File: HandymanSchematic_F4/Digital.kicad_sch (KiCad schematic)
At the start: 39 parts, among them J1 SWD Header, J2 JACKS, J5 ScopeGroundLoop, Q2 2N7002, Q3 2N7002, SW1 RST, SW2 BYP, U3 STM32F411RETx, U4 AMS1117, U5 SSD1306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

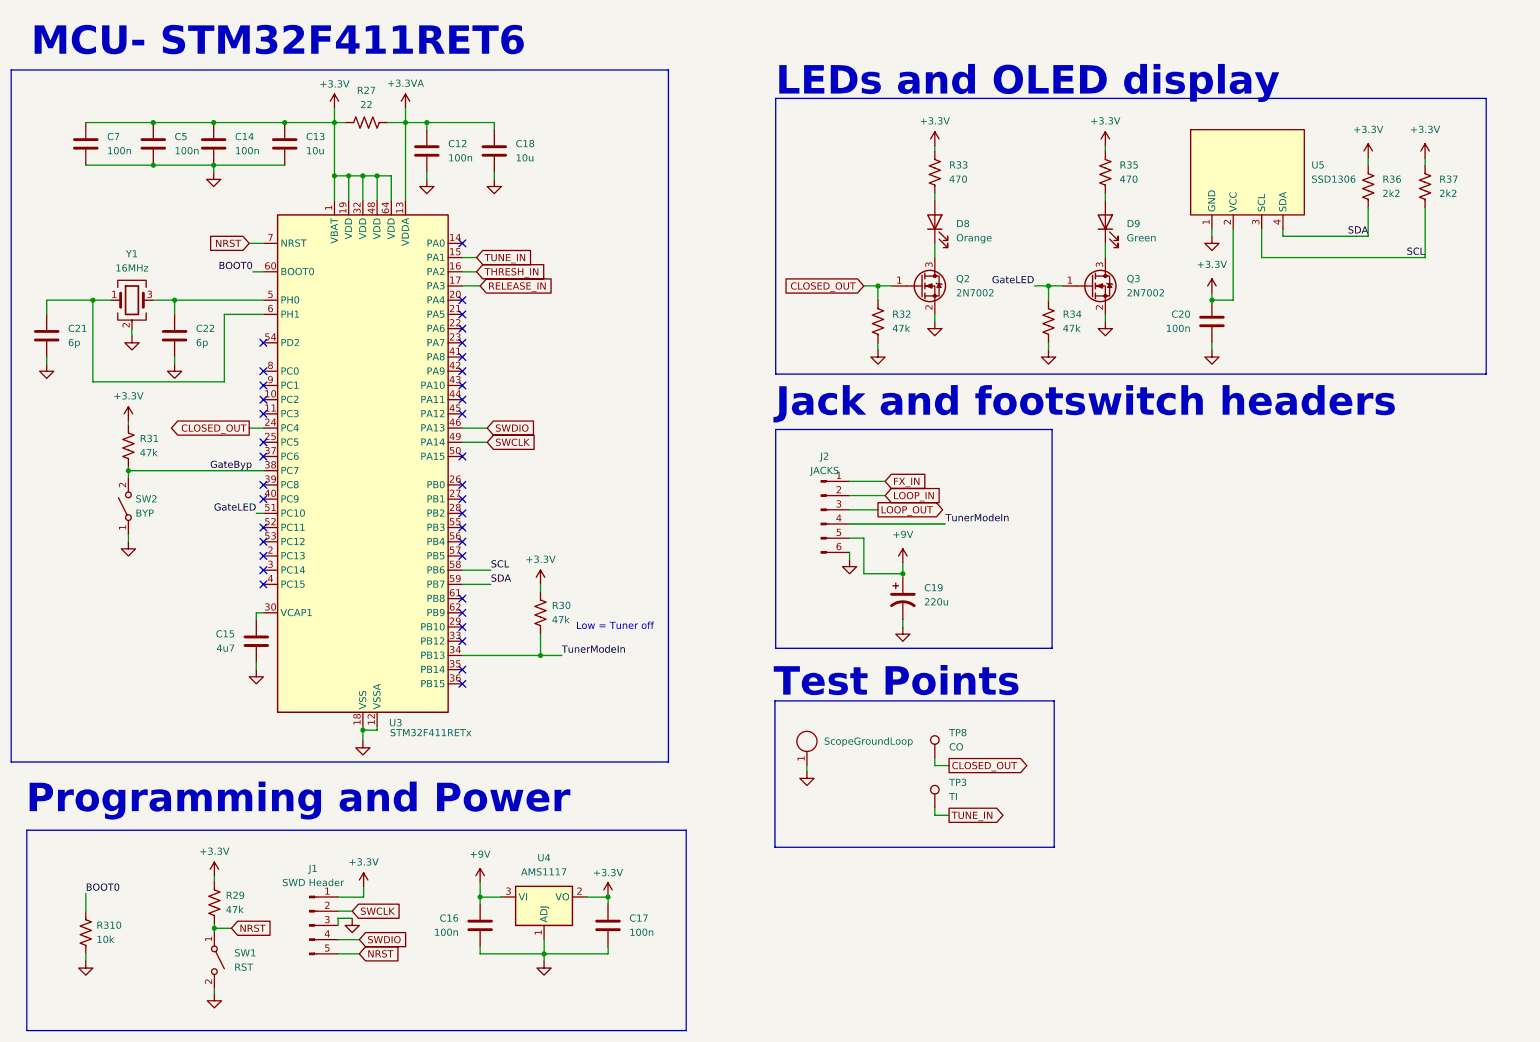
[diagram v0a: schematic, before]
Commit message: schem changes for new display
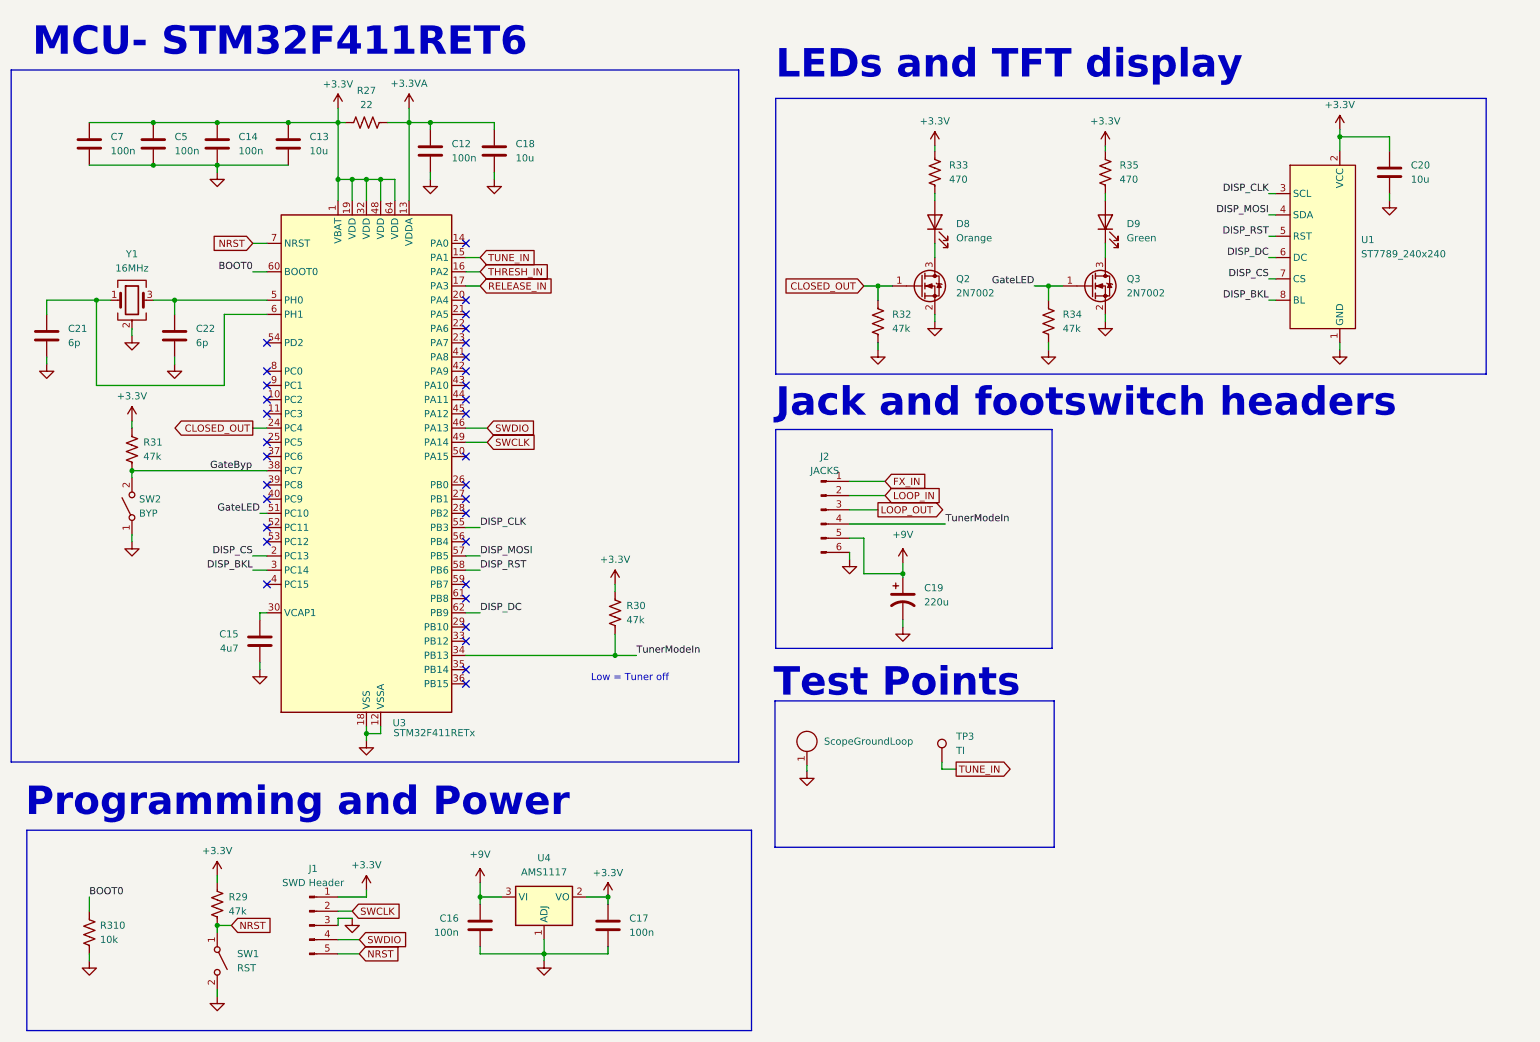
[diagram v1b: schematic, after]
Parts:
- removed R36, R37: 2k2, Resistor_SMD:R_0805_2012Metric, symbol Device:R_US
- removed TP8: CO, TestPoint:TestPoint_THTPad_D2.0mm_Drill1.0mm_VAL, symbol Connector:TestPoint
- removed U5: SSD1306, Display:SSD1306_OLED_128x64_OffBoard, symbol Display_Graphic:SSD1306_OLED_128x64
- added U1: ST7789_240x240, Display:TFT_ST7789_240x240_Breakout, symbol Display_Graphic:TFT_ST7789_240x240_OffBoard
- C20: value 100n -> 10u
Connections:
- net +3.3V: now also U1.2 (VCC)
- net GND: now also U1.1 (GND)
- net DISP_CS: now reaches U3.2 (PC13)
- net DISP_CS: now also U1.7 (CS)
- net DISP_BKL: now reaches U3.3 (PC14)
- net DISP_BKL: now also U1.8 (BL)
- net DISP_CLK: now reaches U3.55 (PB3)
- net DISP_CLK: now also U1.3 (SCL)
- net DISP_MOSI: now reaches U3.57 (PB5)
- net DISP_MOSI: now also U1.4 (SDA)
- net DISP_DC: now reaches U3.62 (PB9)
- net DISP_DC: now also U1.6 (DC)
- net SCL renamed DISP_RST
- net DISP_RST: now also U1.5 (RST)
- net SDA: no longer names the net of U3.59 (PB7)
- no-connect marks 37 -> 33
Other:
- note added: "LEDs and TFT display"
- note removed: "LEDs and OLED display"
- moved on the sheet: C12, C13, C14, C15, C7, R29, R30, R31, R310, SW1, SW2, TP3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

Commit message: beginnings of new layout
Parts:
- J5: footprint Connector_Wire:THT_GND_WIRE -> Connector:THT_GND_WIRE
- SW2: footprint Button_Switch_THT:MiniToggle_SPST -> Button_Switch_THT:SW_TH_Tactile_Omron_B3F-102x
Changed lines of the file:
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@@
 			)
 		)
-		(property "Footprint" "Connector_Wire:THT_GND_WIRE"
+		(property "Footprint" "Connector:THT_GND_WIRE"
 			(at 154.94 139.065 0)
 			(hide yes)
@@
 			)
 		)
-		(property "Footprint" "Button_Switch_THT:MiniToggle_SPST"
+		(property "Footprint" "Button_Switch_THT:SW_TH_Tactile_Omron_B3F-102x"
 			(at 34.29 100.33 0)
 			(hide yes)

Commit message: im routed
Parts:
- removed R30: 47k, Resistor_SMD:R_0805_2012Metric, symbol Device:R_US
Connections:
- net RELEASE_IN: now also U3.16 (PA2); no longer U3.17 (PA3)
- net THRESH_IN: now also U3.17 (PA3); no longer U3.16 (PA2)
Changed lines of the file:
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@@
 	)
 	(junction
-		(at 120.65 127)
-		(diameter 0)
-		(color 0 0 0 0)
-	)
-	(junction
 		(at 76.2 41.91)
 		(diameter 0)
@@
 	(wire
 		(pts
-			(xy 120.65 114.3) (xy 120.65 115.57)
-		)
-		(stroke
-			(width 0)
-			(type default)
-		)
-	)
-	(wire
-		(pts
 			(xy 167.64 60.96) (xy 170.18 60.96)
 		)
@@
 	(wire
 		(pts
-			(xy 93.98 127) (xy 120.65 127)
-		)
-		(stroke
-			(width 0)
-			(type default)
-		)
-	)
-	(wire
-		(pts
 			(xy 165.1 112.395) (xy 172.085 112.395)
 		)
@@
 	(wire
 		(pts
-			(xy 120.65 123.19) (xy 120.65 127)
-		)
-		(stroke
-			(width 0)
-			(type default)
-		)
-	)
-	(wire
-		(pts
 			(xy 93.98 111.76) (xy 96.52 111.76)
 		)
@@
 	(wire
 		(pts
-			(xy 120.65 127) (xy 124.46 127)
+			(xy 93.98 127) (xy 124.46 127)
 		)
 		(stroke
@@
 	(global_label "THRESH_IN"
 		(shape input)
-		(at 96.52 58.42 0)
+		(at 96.52 60.96 0)
 		(fields_autoplaced yes)
 		(effects
@@
 		)
 		(property "Intersheetrefs" "${INTERSHEET_REFS}"
-			(at 109.6652 58.42 0)
+			(at 109.6652 60.96 0)
 			(hide yes)
 			(show_name no)
@@
 	(global_label "RELEASE_IN"
 		(shape input)
-		(at 96.52 60.96 0)
+		(at 96.52 58.42 0)
 		(fields_autoplaced yes)
 		(effects
@@
 		)
 		(property "Intersheetrefs" "${INTERSHEET_REFS}"
-			(at 110.4513 60.96 0)
+			(at 110.4513 58.42 0)
 			(hide yes)
 			(show_name no)
@@
 	)
 	(symbol
-		(lib_id "Device:R_US")
-		(at 120.65 119.38 0)
-		(unit 1)
-		(body_style 1)
-		(exclude_from_sim no)
-		(in_bom yes)
-		(on_board yes)
-		(in_pos_files yes)
-		(dnp no)
-		(fields_autoplaced yes)
-		(property "Reference" "R30"
-			(at 122.682 118.11 0)
-			(show_name no)
-			(do_not_autoplace no)
-			(effects
-				(font
-					(size 1.27 1.27)
-				)
-				(justify left)
-			)
-		)
-		(property "Value" "47k"
-			(at 122.682 120.65 0)
-			(show_name no)
-			(do_not_autoplace no)
-			(effects
-				(font
-					(size 1.27 1.27)
-				)
-				(justify left)
-			)
-		)
-		(property "Footprint" "Resistor_SMD:R_0805_2012Metric"
-			(at 121.666 119.634 90)
-			(hide yes)
-			(show_name no)
-			(do_not_autoplace no)
-			(effects
-				(font
-					(size 1.27 1.27)
-				)
-			)
-		)
-		(property "Datasheet" ""
-			(at 120.65 119.38 0)
-			(hide yes)
-			(show_name no)
-			(do_not_autoplace no)
-			(effects
-				(font
-					(size 1.27 1.27)
-				)
-			)
-		)
-		(property "Description" ""
-			(at 120.65 119.38 0)
-			(hide yes)
-			(show_name no)
-			(do_not_autoplace no)
-			(effects
-				(font
-					(size 1.27 1.27)
-				)
-			)
-		)
-		(pin "1"
-		)
-		(pin "2"
-		)
-		(instances
-			(project "HandymanSchematic_F4"
-				(path "/bc3da82e-d0a7-49a6-b9ec-ecd2040670ff/887caaef-7a77-44c5-aff2-1e54e61c47e4"
-					(reference "R30")
-					(unit 1)
-				)
-			)
-		)
-	)
-	(symbol
 		(lib_id "Device:C")
 		(at 38.1 35.56 180)
@@
 					(unit 1)
 				)
-			)
-		)
-	)
-	(symbol
-		(lib_id "power:+3.3V")
-		(at 120.65 114.3 0)
-		(unit 1)
-		(body_style 1)
-		(exclude_from_sim no)
-		(in_bom yes)
-		(on_board yes)
-		(in_pos_files yes)
-		(dnp no)
-		(fields_autoplaced yes)
-		(property "Reference" "#PWR030"
-			(at 120.65 118.11 0)
-			(hide yes)
-			(show_name no)
-			(do_not_autoplace no)
-			(effects
-				(font
-					(size 1.27 1.27)
-				)
-			)
-		)
-		(property "Value" "+3.3V"
-			(at 120.65 109.855 0)
-			(show_name no)
-			(do_not_autoplace no)
-			(effects
-				(font
-					(size 1.27 1.27)
-				)
-			)
-		)
-		(property "Footprint" ""
-			(at 120.65 114.3 0)
-			(hide yes)
-			(show_name no)
-			(do_not_autoplace no)
-			(effects
-				(font
-					(size 1.27 1.27)
-				)
-			)
-		)
-		(property "Datasheet" ""
-			(at 120.65 114.3 0)
-			(hide yes)
-			(show_name no)
-			(do_not_autoplace no)
-			(effects
-				(font
-					(size 1.27 1.27)
-				)
-			)
-		)
-		(property "Description" ""
-			(at 120.65 114.3 0)
-			(hide yes)
-			(show_name no)
-			(do_not_autoplace no)
-			(effects
-				(font
-					(size 1.27 1.27)
-				)
-			)
-		)
-		(pin "1"
-		)
-		(instances
-			(project "HandymanSchematic_F4"
-				(path "/bc3da82e-d0a7-49a6-b9ec-ecd2040670ff/887caaef-7a77-44c5-aff2-1e54e61c47e4"
-					(reference "#PWR030")
-					(unit 1)
-				)

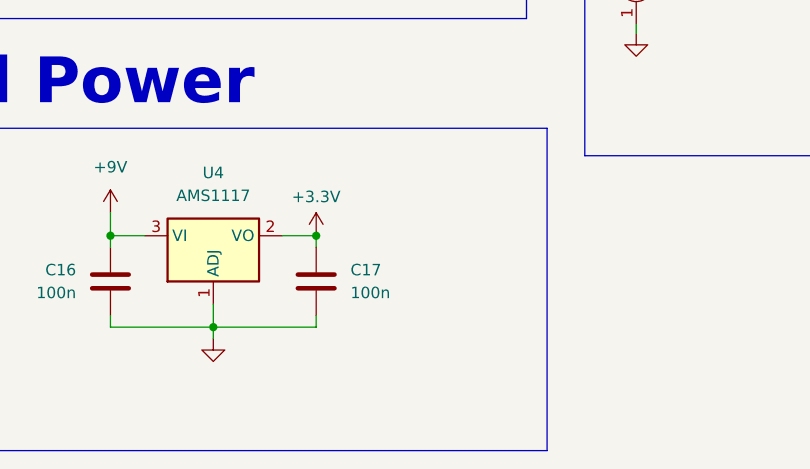
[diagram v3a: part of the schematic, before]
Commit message: corner bevels, silkscreen spacing
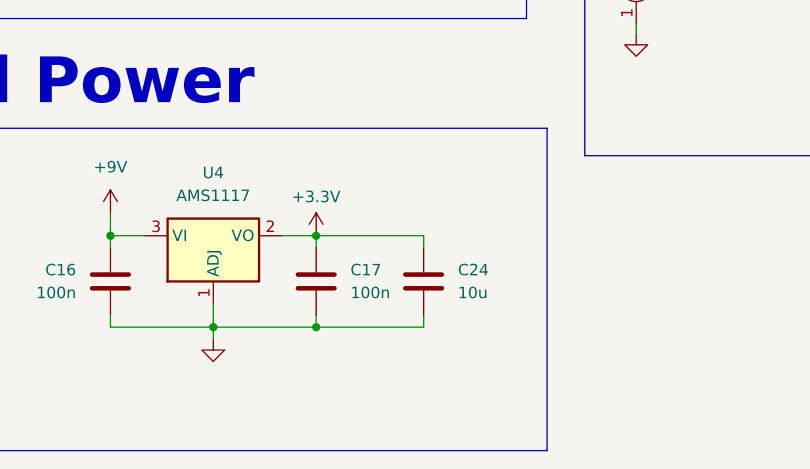
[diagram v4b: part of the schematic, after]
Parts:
- added C24: 10u, Capacitor_SMD:C_0805_2012Metric, symbol Device:C
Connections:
- net +3.3V: now also C24.2
- net GND: now also C24.1
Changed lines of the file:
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@@
 	)
 	(junction
+		(at 119.38 180.34)
+		(diameter 0)
+		(color 0 0 0 0)
+	)
+	(junction
 		(at 83.82 31.75)
 		(diameter 0)
@@
 	(wire
 		(pts
+			(xy 131.318 170.18) (xy 119.38 170.18)
+		)
+		(stroke
+			(width 0)
+			(type default)
+		)
+	)
+	(wire
+		(pts
 			(xy 19.05 66.04) (xy 19.05 63.5)
 		)
@@
 	(wire
 		(pts
+			(xy 131.318 180.34) (xy 119.38 180.34)
+		)
+		(stroke
+			(width 0)
+			(type default)
+		)
+	)
+	(wire
+		(pts
 			(xy 71.12 173.99) (xy 73.66 173.99)
 		)
@@
 	(wire
 		(pts
+			(xy 131.318 171.45) (xy 131.318 170.18)
+		)
+		(stroke
+			(width 0)
+			(type default)
+		)
+	)
+	(wire
+		(pts
 			(xy 57.15 119.38) (xy 57.15 120.65)
 		)
@@
 	(wire
 		(pts
+			(xy 131.318 179.07) (xy 131.318 180.34)
+		)
+		(stroke
+			(width 0)
+			(type default)
+		)
+	)
+	(wire
+		(pts
 			(xy 83.82 31.75) (xy 80.01 31.75)
 		)
@@
 					(unit 1)
 				)
+			)
+		)
+	)
+	(symbol
+		(lib_id "Device:C")
+		(at 131.318 175.26 180)
+		(unit 1)
+		(body_style 1)
+		(exclude_from_sim no)
+		(in_bom yes)
+		(on_board yes)
+		(in_pos_files yes)
+		(dnp no)
+		(property "Reference" "C24"
+			(at 135.128 173.99 0)
+			(show_name no)
+			(do_not_autoplace no)
+			(effects
+				(font
+					(size 1.27 1.27)
+				)
+				(justify right)
+			)
+		)
+		(property "Value" "10u"
+			(at 135.128 176.53 0)
+			(show_name no)
+			(do_not_autoplace no)
+			(effects
+				(font
+					(size 1.27 1.27)
+				)
+				(justify right)
+			)
+		)
+		(property "Footprint" "Capacitor_SMD:C_0805_2012Metric"
+			(at 130.3528 171.45 0)
+			(hide yes)
+			(show_name no)
+			(do_not_autoplace no)
+			(effects
+				(font
+					(size 1.27 1.27)
+				)
+			)
+		)
+		(property "Datasheet" ""
+			(at 131.318 175.26 0)
+			(hide yes)
+			(show_name no)
+			(do_not_autoplace no)
+			(effects
+				(font
+					(size 1.27 1.27)
+				)
+			)
+		)
+		(property "Description" ""
+			(at 131.318 175.26 0)
+			(hide yes)
+			(show_name no)
+			(do_not_autoplace no)
+			(effects
+				(font
+					(size 1.27 1.27)
+				)
+			)
+		)
+		(pin "1"
+		)
+		(pin "2"
+		)
+		(instances
+			(project "HandymanSchematic_F4"
+				(path "/bc3da82e-d0a7-49a6-b9ec-ecd2040670ff/887caaef-7a77-44c5-aff2-1e54e61c47e4"
+					(reference "C24")
+					(unit 1)
+				)

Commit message: rev3 sent to fab
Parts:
- removed J2: JACKS, Connector_PinHeader_2.54mm:PinHeader_1x06_P2.54mm_Vertical, symbol Connector:Conn_01x06_Pin
- added J2: Jacks, Connector_PinSocket_2.54mm:PinSocket_1x07_P2.54mm_Vertical, symbol Connector:Conn_01x07_Pin
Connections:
- net +9V: now also J2.6 (Pin_6)
- net FX_IN: now also J2.1 (Pin_1)
- net GND: now also J2.5 (Pin_5), J2.7 (Pin_7)
- net LOOP_IN: now also J2.2 (Pin_2)
- net LOOP_OUT: now also J2.3 (Pin_3)
- net TunerModeIn: now also J2.4 (Pin_4)
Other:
- moved on the sheet: C19
